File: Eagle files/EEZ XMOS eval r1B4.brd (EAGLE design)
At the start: 100 x 85 mm, 227 parts, among them IC1 TPS61169DCKR, IC10 IS42S16400J, IC11 SN74CBTLV3257, IC12 SN74LVC1G02DBVR, IC13 AT25SF041-SSHDT, IC14 SN74CBTLV3257, IC15 TPS2051BDBVR, IC16 TPD2E001DZDR, IC17 TPS561208DDCR, IC18 XE216-512-TQ128-C20, IC19 TPD4E001DRLR, IC2 TPS561208DDCR, IC20 TPD4E001DRLR, IC21 74LVC1G07SE-7, IC22 74LVC1G07SE-7, IC23 TPA6205A1DGN, IC24 DP83848CVV/NOPB, IC25 M95256-WMN6P, IC26 74VHC595MTC, IC27 PCA21125T/Q900/1,1, IC28 MCP23S17-E/SS, IC3 74VHC595MTC, IC4 TPS561208DDCR, IC5 74VHC595MTC, IC6 TPS3808G33DBVR, IC7 AR1021-I/SS, IC8 TPS3808G09DBVR, IC9 74AUP1G74DC.125, J1 678038020, J2 5033981892, Q1 IRLML2246TRPBF, SW1 1301.9316, X1 FC68149, X2 SSW-105-02-S-D, X3 TSW-104-02-S-D_NN, X4 TSW-103-07-F-D, X5 ZL231-20KG, X6 22-23-2021, X7 LMJTAB881243M-L, X8 SSW-107-02-S-D, X9 PCA-6G-20-HL-3 or 52746-2071, Y1 XTAL016178- 85SMX

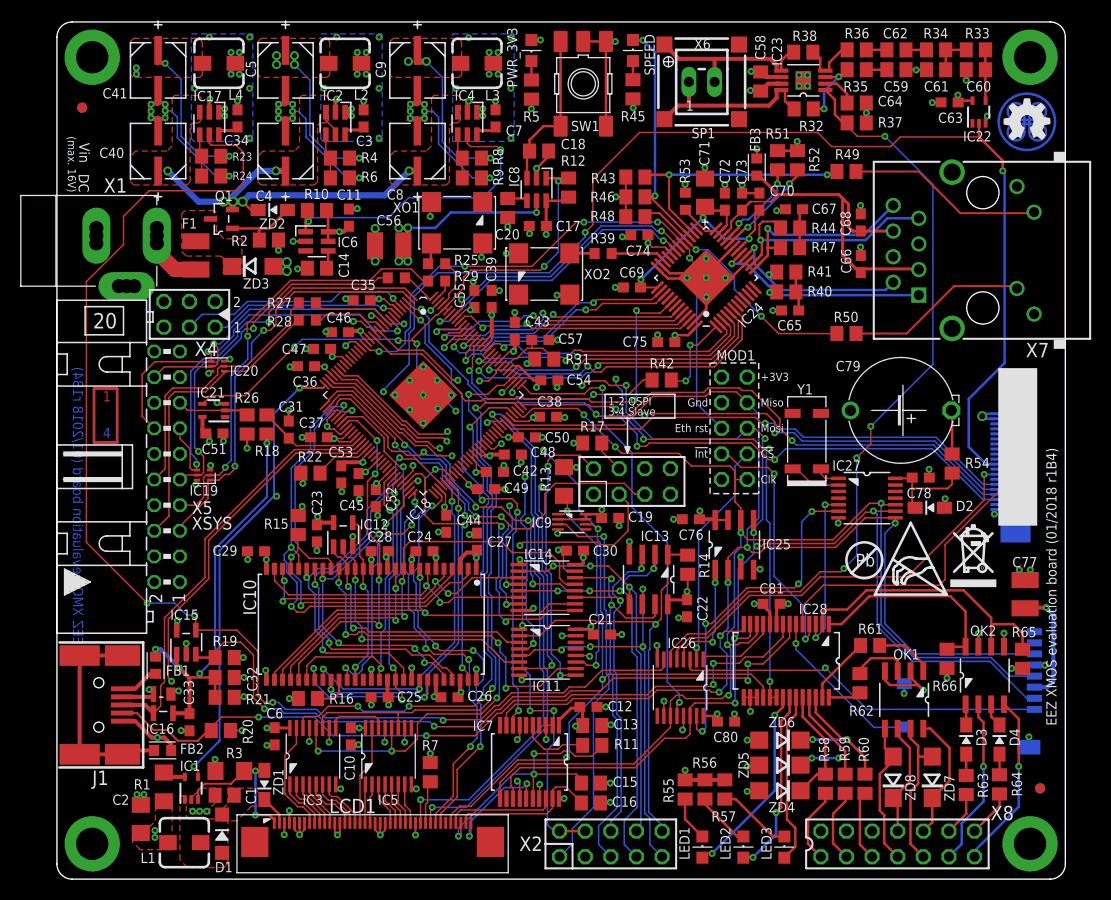
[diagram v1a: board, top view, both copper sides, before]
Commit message: BOM first version, added R67 as test point
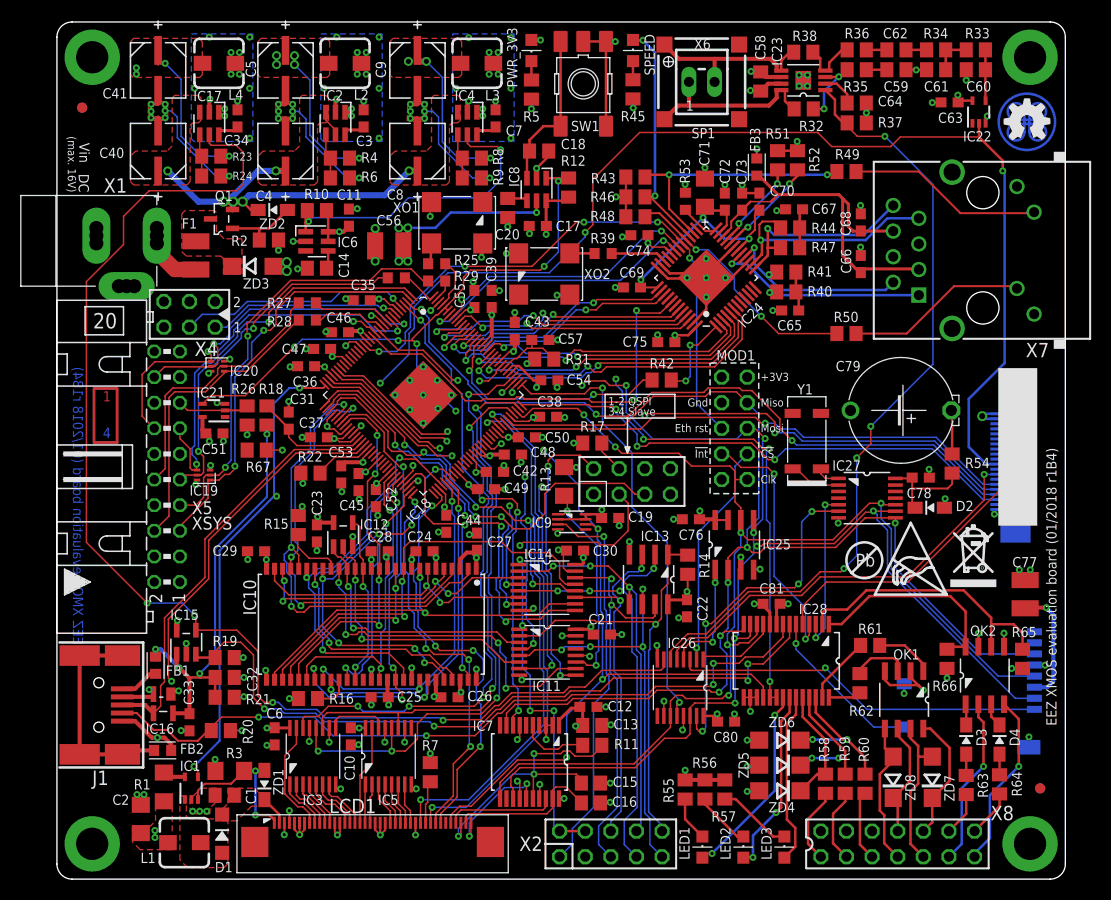
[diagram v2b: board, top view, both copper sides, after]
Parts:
- added R67: 0R, rcl:R0805
- moved C31 0.89 mm to (23.0, 45.5)
- moved R18 0.89 mm to (20.8, 46.0)
- moved R26 0.89 mm to (18.9, 46.0)
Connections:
- new net N$18: IC18.43, R67.1
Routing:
- net N$18: track 0.00 -> 11.5 mm, vias 0 -> 2
- net SPI1_MISO: track 127.5 -> 122.8 mm
- net SPI1_MOSI: track 141.4 -> 137.6 mm
- net SPI1_CLK: track 129.9 -> 126.0 mm
- net !RIVERDI_INT: track 30.7 -> 28.7 mm
- net ETH_MDC: track 29.4 -> 28.5 mm
- net USB_VBUS: track 44.5 -> 45.4 mm
- net !QSPI_SEL: track 34.5 -> 33.6 mm
- net N$43: track 10.7 -> 11.5 mm
- net SD_ADQ7: track 35.0 -> 35.7 mm
- net TCK: track 36.6 -> 35.9 mm
- net X0D11/LCD_BR: track 87.8 -> 88.4 mm
- net ETH_RST: track 60.5 -> 59.9 mm
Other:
- board text removed: "C1"
- board text removed: "C10"
- board text removed: "C11"
- board text removed: "C12"
- board text removed: "C13"
- board text removed: "C14"
- board text removed: "C15"
- board text removed: "C16"
- board text removed: "C17"
- board text removed: "C18"
- board text removed: "C19"
- board text removed: "C2"
- board text removed: "C20"
- board text removed: "C21"
- board text removed: "C22"
- board text removed: "C23"
- board text removed: "C24"
- board text removed: "C25"
- board text removed: "C26"
- board text removed: "C27"
- board text removed: "C28"
- board text removed: "C29"
- board text removed: "C3"
- board text removed: "C30"
- board text removed: "C31"
- board text removed: "C32"
- board text removed: "C33"
- board text removed: "C34"
- board text removed: "C35"
- board text removed: "C36"
- board text removed: "C37"
- board text removed: "C38"
- board text removed: "C39"
- board text removed: "C4"
- board text removed: "C40"
- board text removed: "C41"
- board text removed: "C42"
- board text removed: "C43"
- board text removed: "C44"
- board text removed: "C45"
- board text removed: "C46"
- board text removed: "C47"
- board text removed: "C48"
- board text removed: "C49"
- board text removed: "C5"
- board text removed: "C50"
- board text removed: "C51"
- board text removed: "C52"
- board text removed: "C53"
- board text removed: "C54"
- board text removed: "C55"
- board text removed: "C56"
- board text removed: "C57"
- board text removed: "C58"
- board text removed: "C59"
- board text removed: "C6"
- board text removed: "C60"
- board text removed: "C61"
- board text removed: "C62"
- board text removed: "C63"
- board text removed: "C64"
- board text removed: "C65"
- board text removed: "C66"
- board text removed: "C67"
- board text removed: "C68"
- board text removed: "C69"
- board text removed: "C7"
- board text removed: "C70"
- board text removed: "C71"
- board text removed: "C72"
- board text removed: "C73"
- board text removed: "C74"
- board text removed: "C75"
- board text removed: "C76"
- board text removed: "C77"
- board text removed: "C78"
- board text removed: "C79"
- board text removed: "C8"
- board text removed: "C80"
- board text removed: "C81"
- board text removed: "C9"
- board text removed: "D1"
- board text removed: "D2"
- board text removed: "D3"
- board text removed: "D4"
- board text removed: "F1"
- board text removed: "FB1"
- board text removed: "FB2"
- board text removed: "FB3"
- board text removed: "IC1"
- board text removed: "IC10"
- board text removed: "IC11"
- board text removed: "IC12"
- board text removed: "IC13"
- board text removed: "IC14"
- board text removed: "IC15"
- board text removed: "IC16"
- board text removed: "IC17"
- board text removed: "IC18"
- board text removed: "IC19"
- board text removed: "IC2"
- board text removed: "IC20"
- board text removed: "IC21"
- board text removed: "IC22"
- board text removed: "IC23"
- board text removed: "IC24"
- board text removed: "IC25"
- board text removed: "IC26"
- board text removed: "IC27"
- board text removed: "IC28"
- board text removed: "IC3"
- board text removed: "IC4"
- board text removed: "IC5"
- board text removed: "IC6"
- board text removed: "IC7"
- board text removed: "IC8"
- board text removed: "IC9"
- board text removed: "J1"
- board text removed: "J2"
- board text removed: "L1"
- board text removed: "L2"
- board text removed: "L3"
- board text removed: "L4"
- board text removed: "LCD1"
- board text removed: "LED1"
- board text removed: "LED2"
- board text removed: "LED3"
- board text removed: "MOD1"
- board text removed: "OK1"
- board text removed: "OK2"
- board text removed: "PWR_3V3"
- board text removed: "Q1"
- board text removed: "R1"
- board text removed: "R10"
- board text removed: "R11"
- board text removed: "R12"
- board text removed: "R13"
- board text removed: "R14"
- board text removed: "R15"
- board text removed: "R16"
- board text removed: "R17"
- board text removed: "R18"
- board text removed: "R19"
- board text removed: "R2"
- board text removed: "R20"
- board text removed: "R21"
- board text removed: "R22"
- board text removed: "R23"
- board text removed: "R24"
- board text removed: "R25"
- board text removed: "R26"
- board text removed: "R27"
- board text removed: "R28"
- board text removed: "R29"
- board text removed: "R3"
- board text removed: "R31"
- board text removed: "R32"
- board text removed: "R33"
- board text removed: "R34"
- board text removed: "R35"
- board text removed: "R36"
- board text removed: "R37"
- board text removed: "R38"
- board text removed: "R39"
- board text removed: "R4"
- board text removed: "R40"
- board text removed: "R41"
- board text removed: "R42"
- board text removed: "R43"
- board text removed: "R44"
- board text removed: "R45"
- board text removed: "R46"
- board text removed: "R47"
- board text removed: "R48"
- board text removed: "R49"
- board text removed: "R5"
- board text removed: "R50"
- board text removed: "R51"
- board text removed: "R52"
- board text removed: "R53"
- board text removed: "R54"
- board text removed: "R55"
- board text removed: "R56"
- board text removed: "R57"
- board text removed: "R58"
- board text removed: "R59"
- board text removed: "R6"
- board text removed: "R60"
- board text removed: "R61"
- board text removed: "R62"
- board text removed: "R63"
- board text removed: "R64"
- board text removed: "R65"
- board text removed: "R66"
- board text removed: "R7"
- board text removed: "R8"
- board text removed: "R9"
- board text removed: "SP1"
- board text removed: "SPEED"
- board text removed: "SW1"
- board text removed: "X1"
- board text removed: "X2"
- board text removed: "X4"
- board text removed: "X5"
- board text removed: "X6"
- board text removed: "X7"
- board text removed: "X8"
- board text removed: "X9"
- board text removed: "XO1"
- board text removed: "XO2"
- board text removed: "Y1"
- board text removed: "ZD1"
- board text removed: "ZD2"
- board text removed: "ZD3"
- board text removed: "ZD4"
- board text removed: "ZD5"
- board text removed: "ZD6"
- board text removed: "ZD7"
- board text removed: "ZD8"

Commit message: .brd file optimization
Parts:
- removed IC25: M95256-WMN6P, MyLib6:SOIC127P600X175-8N
- added IC29: M95256-WMN6P, EEZ_Lib1:SOIC127P600X175-8N
- FB1, FB2, FB3: device MyLib6:BEAD0603 -> EEZ_Lib1:BEAD0603
- IC27: device MyLib6:SOP65P640X120-14N -> EEZ_Lib1:SOP65P640X120-14N
- Q1: device MyLib6:SOT95P237X112-3N -> EEZ_Lib1:SOT95P237X112-3N
- moved FB1 0.13 mm to (9.78, 21.3)
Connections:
- net !SPI1_EEPROM: now also IC29.1; no longer IC25.1
- net +3V3: now also IC29.3, IC29.7, IC29.8; no longer IC25.3, IC25.7, IC25.8
- net GND: now also IC29.4; no longer IC25.4
- net SPI1_CLK: now also IC29.6; no longer IC25.6
- net SPI1_MISO: now also IC29.2; no longer IC25.2
- net SPI1_MOSI: now also IC29.5; no longer IC25.5
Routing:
- net XL_DN1: track 31.6 -> 35.6 mm
- net USB_D_N: track 41.6 -> 44.1 mm
- net XL_UP0: track 27.1 -> 29.0 mm
- net N$37: track 22.6 -> 23.4 mm
